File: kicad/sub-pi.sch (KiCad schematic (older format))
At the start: 18 parts, among them J2 RPI, Q1 AO3404 (Q_NMOS_GSD), Q2 AO3404 (Q_NMOS_GSD), U3 NCP1117-5.0_TO252, U4 NCP1117-3.3_TO252, U5 NCP1117-5.0_TO252, U6 NCP1117-3.3_TO252, U7 SI9933ADY

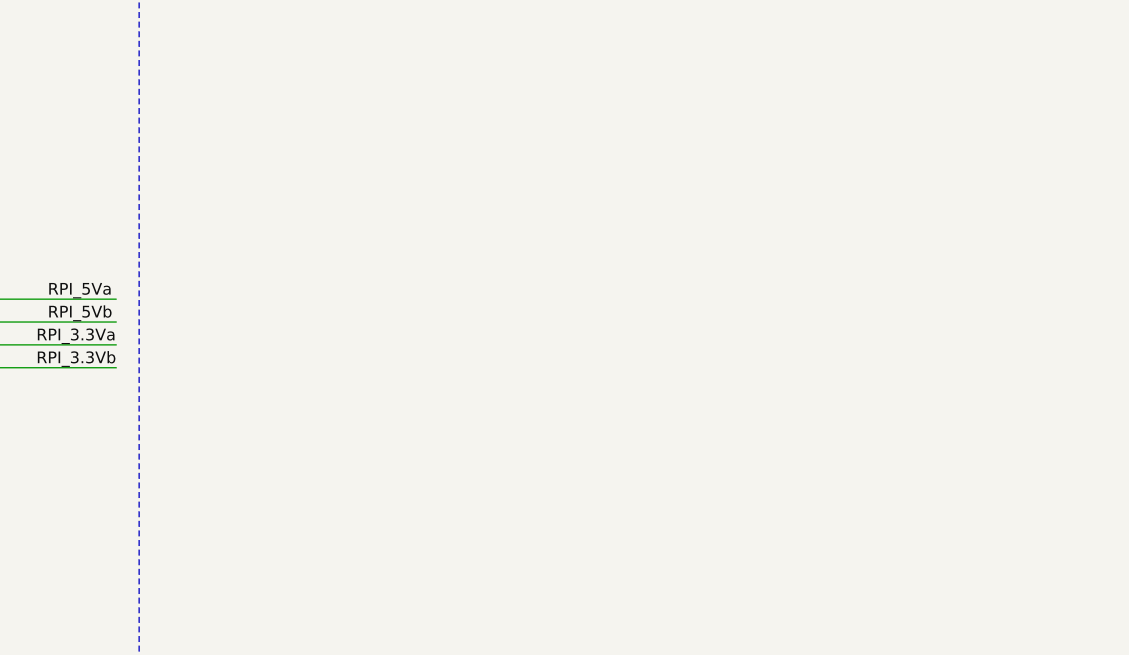
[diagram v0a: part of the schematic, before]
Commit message: Added LTC1154 to schematic.
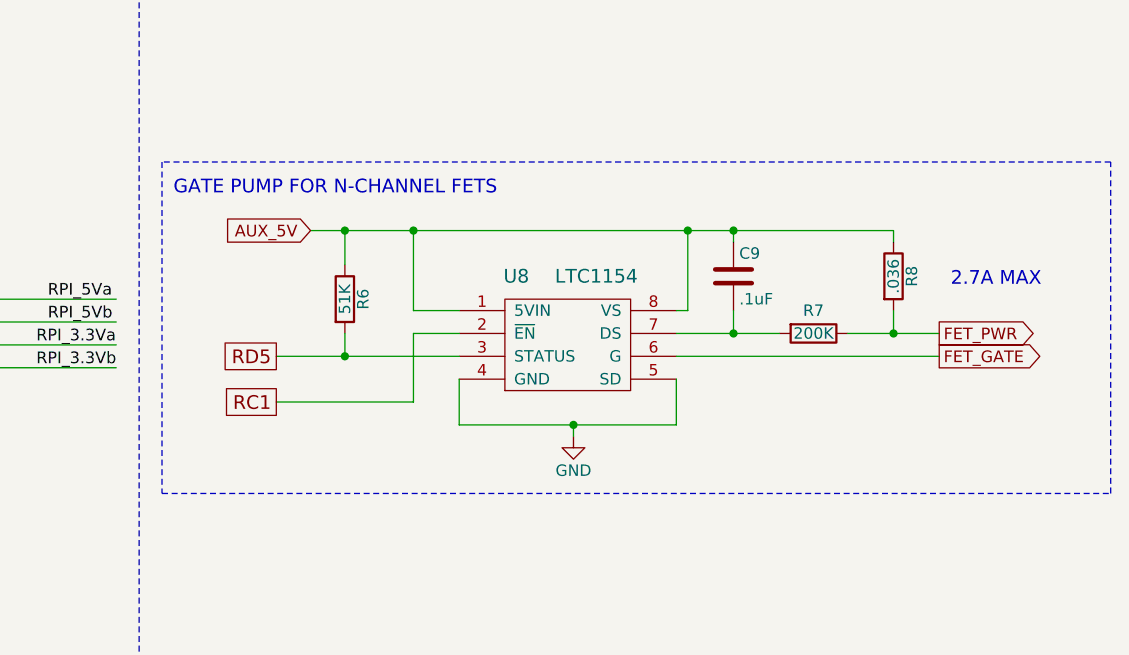
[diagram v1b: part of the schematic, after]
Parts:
- added C9: .1uF, symbol C
- added R6: 51K, symbol R
- added R7: 200K, symbol R
- added R8: .036, symbol R
- added U8: LTC1154, symbol LTC1154
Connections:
- net labels added: FET_GATE, FET_PWR, RC1, RD5
- wire segments 76 -> 98
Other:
- note added: "2.7A MAX"
- note added: "GATE PUMP FOR N-CHANNEL FETS"
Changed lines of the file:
@@
 	1    0    0    -1
+$EndComp
+Text Notes 650  4100 0    60   ~ 0
+STANDBY & RPI SWITCHED POWER\n
+Text Notes 750  6950 0    60   ~ 0
+3.3V output from\nmicrocontroller
+Text Notes 800  4550 0    60   ~ 0
+20VDC Max
+Text GLabel 7600 5200 0    51   Input ~ 0
+AUX_5V
+$Comp
+L LTC1154 U8
+U 1 1 5A652C0F
+P 8750 5700
+F 0 "U8" H 8500 6000 60  0000 C CNN
+F 1 "LTC1154" H 8850 6000 60  0000 C CNN
+F 2 "" H 8750 5700 60  0001 C CNN
+F 3 "" H 8750 5700 60  0001 C CNN
+	1    8750 5700
+	1    0    0    -1
+$EndComp
+$Comp
+L R R6
+U 1 1 5A652E3D
+P 7750 5500
+F 0 "R6" V 7830 5500 50  0000 C CNN
+F 1 "51K" V 7750 5500 50  0000 C CNN
+F 2 "" V 7680 5500 50  0001 C CNN
+F 3 "" H 7750 5500 50  0001 C CNN
+	1    7750 5500
+	1    0    0    -1
+$EndComp
+Text GLabel 7450 5950 0    60   UnSpc ~ 0
+RC1
+$Comp
+L GND #PWR031
+U 1 1 5A65318B
+P 8750 6100
+F 0 "#PWR031" H 8750 5850 50  0001 C CNN
+F 1 "GND" H 8750 5950 50  0000 C CNN
+F 2 "" H 8750 6100 50  0001 C CNN
+F 3 "" H 8750 6100 50  0001 C CNN
+	1    8750 6100
+	1    0    0    -1
+$EndComp
+$Comp
+L C C9
+U 1 1 5A65333A
+P 9450 5400
+F 0 "C9" H 9475 5500 50  0000 L CNN
+F 1 ".1uF" H 9475 5300 50  0000 L CNN
+F 2 "" H 9488 5250 50  0001 C CNN
+F 3 "" H 9450 5400 50  0001 C CNN
+	1    9450 5400
+	1    0    0    -1
+$EndComp
+$Comp
+L R R8
+U 1 1 5A6533A2
+P 10150 5400
+F 0 "R8" V 10230 5400 50  0000 C CNN
+F 1 ".036" V 10150 5400 50  0000 C CNN
+F 2 "" V 10080 5400 50  0001 C CNN
+F 3 "" H 10150 5400 50  0001 C CNN
+	1    10150 5400
+	1    0    0    -1
+$EndComp
+$Comp
+L R R7
+U 1 1 5A6537CB
+P 9800 5650
+F 0 "R7" V 9700 5650 50  0000 C CNN
+F 1 "200K" V 9800 5650 50  0000 C CNN
+F 2 "" V 9730 5650 50  0001 C CNN
+F 3 "" H 9800 5650 50  0001 C CNN
+	1    9800 5650
+	0    1    1    0
 $EndComp
 Wire Wire Line
@@
 Wire Notes Line
 	6850 7700 550  7700
-Text Notes 650  4100 0    60   ~ 0
-STANDBY & RPI SWITCHED POWER\n
 Connection ~ 1400 5700
 Connection ~ 1400 4950
@@
 Wire Notes Line
 	550  7700 550  3950
-Text Notes 750  6950 0    60   ~ 0
-3.3V output from\nmicrocontroller
-Text Notes 800  4550 0    60   ~ 0
-20VDC Max
+Wire Wire Line
+	7600 5200 10150 5200
+Wire Wire Line
+	7750 5200 7750 5350
+Wire Wire Line
+	7750 5650 7750 5750
+Wire Wire Line
+	7450 5750 8250 5750
+Wire Wire Line
+	8250 5550 8050 5550
+Wire Wire Line
+	8050 5550 8050 5200
+Connection ~ 7750 5200
+Wire Wire Line
+	7450 5950 8050 5950
+Wire Wire Line
+	8050 5950 8050 5650
+Wire Wire Line
+	8050 5650 8250 5650
+Wire Wire Line
+	8250 5850 8250 6050
+Wire Wire Line
+	8750 6050 8750 6100
+Connection ~ 8750 6050
+Connection ~ 8050 5200
+Connection ~ 9450 5200
+Wire Wire Line
+	9200 5550 9250 5550
+Wire Wire Line
+	9250 5550 9250 5200
+Connection ~ 9250 5200
+Wire Wire Line
+	9200 5650 9650 5650
+Connection ~ 9450 5650
+Wire Wire Line
+	9450 5650 9450 5550
+Wire Wire Line
+	9450 5250 9450 5200
+Wire Wire Line
+	10150 5200 10150 5250
+Wire Wire Line
+	10150 5550 10150 5650
+Wire Wire Line
+	9950 5650 10350 5650
+Text GLabel 7450 5750 0    60   UnSpc ~ 0
+RD5
+Connection ~ 7750 5750
+Text GLabel 10350 5750 2    51   Output ~ 0
+FET_GATE
+Wire Wire Line
+	10350 5750 9200 5750
+Text GLabel 10350 5650 2    51   Output ~ 0
+FET_PWR
+Connection ~ 10150 5650
+Wire Notes Line
+	6950 4900 6950 6350
+Wire Notes Line
+	6950 6350 11100 6350
+Wire Notes Line
+	11100 6350 11100 4900
+Wire Notes Line
+	11100 4900 6950 4900
+Text Notes 7000 5050 0    60   ~ 0
+GATE PUMP FOR N-CHANNEL FETS
+Wire Wire Line
+	9200 6050 9200 5850
+Wire Wire Line
+	8250 6050 9200 6050
+Text Notes 10400 5450 0    60   ~ 0
+2.7A MAX
 $EndSCHEMATC

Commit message: Media migration.
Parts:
- added R10, R11, R12, R13, R14, R15, R16, R17, R9: 0, symbol R
- added R? (x2): 10K, symbol R
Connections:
- net labels added: +3.3V, PISPICLK, PISPIDIN, PISPIDOUT, PISPI~SS~, RB0, RB1, RB2, RB3, RB4, RB5, RE0, RE1, RE2
- wire segments 98 -> 134
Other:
- moved on the sheet: J2
